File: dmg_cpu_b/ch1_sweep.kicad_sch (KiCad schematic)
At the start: 109 parts

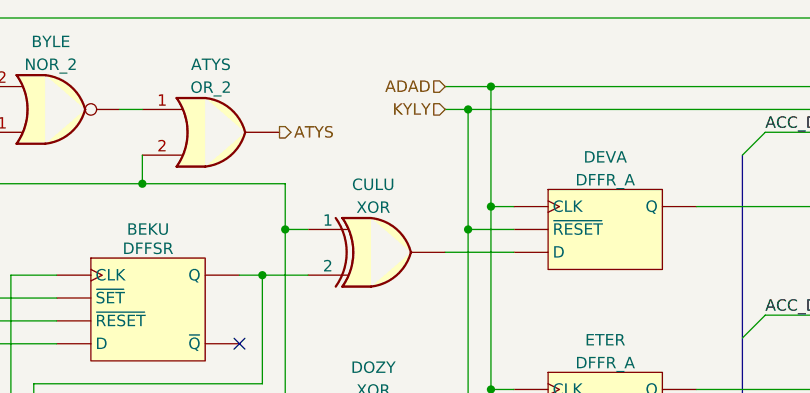
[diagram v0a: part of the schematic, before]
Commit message: Channel 2 + Channel 3 added. Channel 3 fits on 2 sheets.
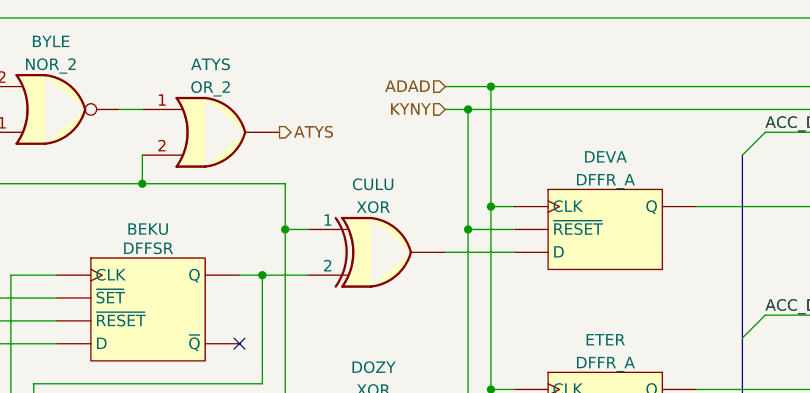
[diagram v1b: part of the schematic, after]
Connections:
- net KYLY renamed KYNY
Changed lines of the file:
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@@
     (effects (font (size 1.27 1.27)) (justify left))
   )
-  (hierarchical_label "KYLY" (shape input) (at 246.38 23.495 180)
+  (hierarchical_label "KYNY" (shape input) (at 246.38 23.495 180)
     (effects (font (size 1.27 1.27)) (justify right))
   )

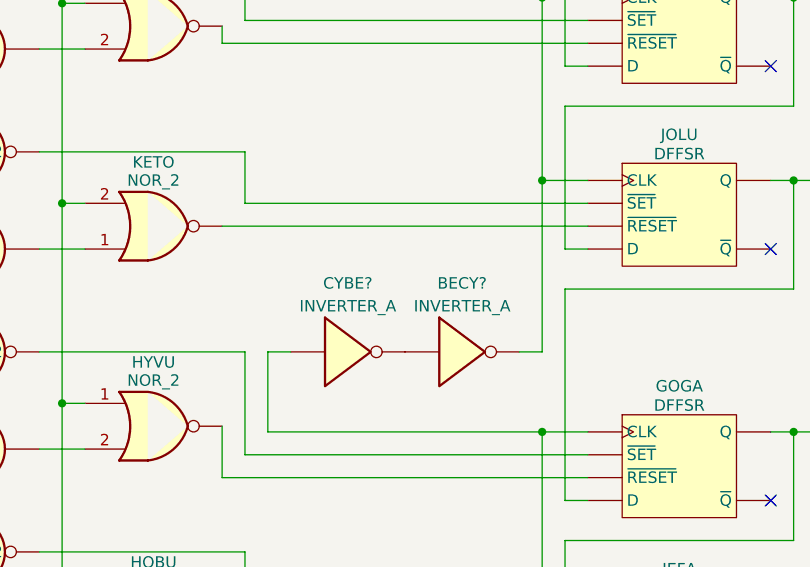
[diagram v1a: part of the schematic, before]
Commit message: fixes made following review
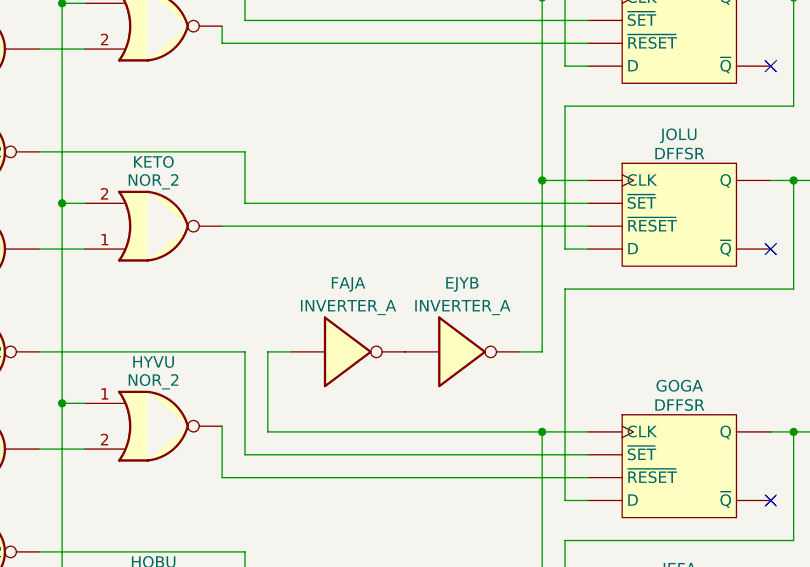
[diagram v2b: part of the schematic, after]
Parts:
- gave numbers to parts that had none: 2
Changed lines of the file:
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@@
   (symbol (lib_id "DMG_CPU_Cells:INVERTER_A") (at 176.53 210.82 0) (unit 1)
     (in_bom yes) (on_board yes)
-    (property "Reference" "CYBE?" (id 0) (at 176.53 203.2 0))
+    (property "Reference" "FAJA" (id 0) (at 176.53 203.2 0))
     (property "Value" "INVERTER_A" (id 1) (at 176.53 205.74 0))
     (property "Footprint" "" (id 2) (at 173.99 210.82 0)
@@
   (symbol (lib_id "DMG_CPU_Cells:INVERTER_A") (at 189.23 210.82 0) (unit 1)
     (in_bom yes) (on_board yes)
-    (property "Reference" "BECY?" (id 0) (at 189.23 203.2 0))
+    (property "Reference" "EJYB" (id 0) (at 189.23 203.2 0))
     (property "Value" "INVERTER_A" (id 1) (at 189.23 205.74 0))
     (property "Footprint" "" (id 2) (at 186.69 210.82 0)

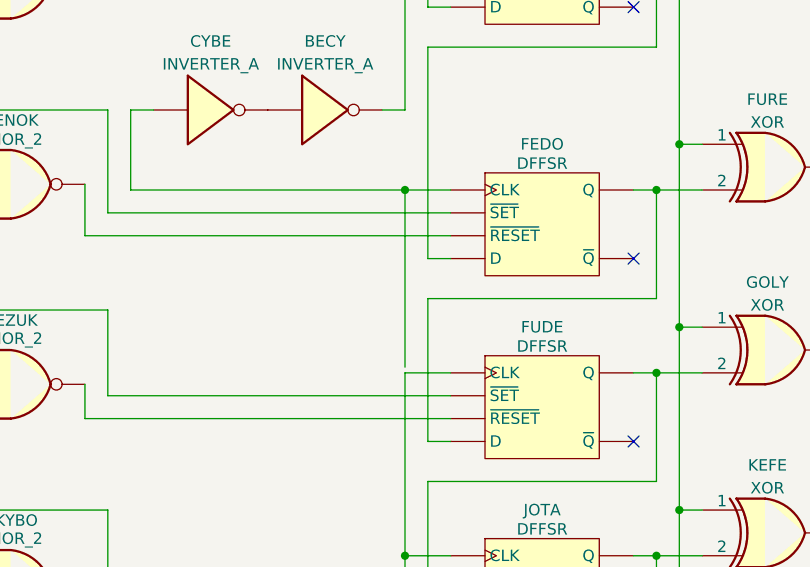
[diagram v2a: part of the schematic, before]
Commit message: Fixes made from issues, channel 4 sheet aded and tidy up of hierarchical APU sheet. Small fixes done here and there when doing ERC.
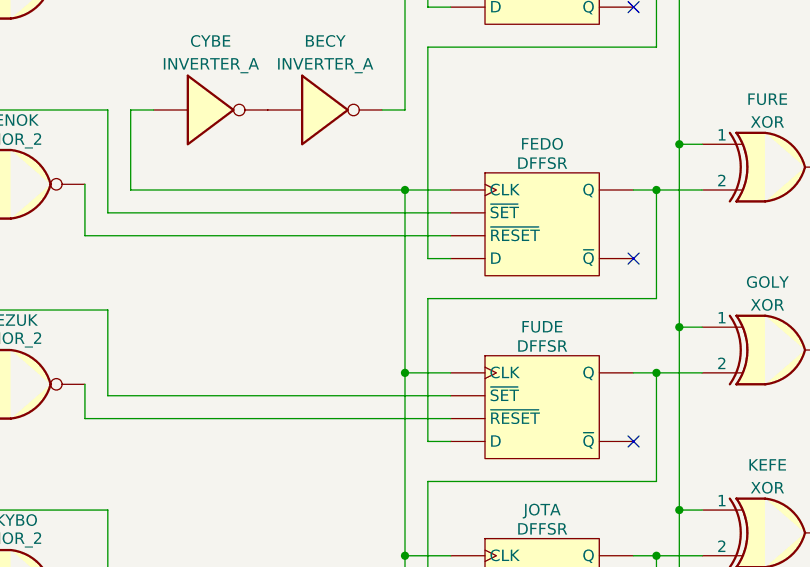
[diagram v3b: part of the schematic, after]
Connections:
- net at CYBE.1, FEDO.7 (CLK): now also EJYB.2, FUDE.7 (CLK), JOLU.7 (CLK), JOTA.7 (CLK)
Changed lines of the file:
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@@
   (junction (at 294.005 81.915) (diameter 0) (color 0 0 0 0)
+  )
+  (junction (at 198.12 151.13) (diameter 0) (color 0 0 0 0)
   )
   (junction (at 294.005 61.595) (diameter 0) (color 0 0 0 0)
@@
     (stroke (width 0) (type default) (color 0 0 0 0))
   )
-  (wire (pts (xy 198.12 130.81) (xy 198.12 150.495))
+  (wire (pts (xy 198.12 130.81) (xy 198.12 151.13))
     (stroke (width 0) (type default) (color 0 0 0 0))
   )
@@
   (symbol (lib_id "power:GND") (at 192.405 52.07 0) (unit 1)
     (in_bom yes) (on_board yes) (fields_autoplaced)
-    (property "Reference" "#PWR?" (id 0) (at 192.405 58.42 0)
+    (property "Reference" "#PWR0108" (id 0) (at 192.405 58.42 0)
       (effects (font (size 1.27 1.27)) hide)
     )

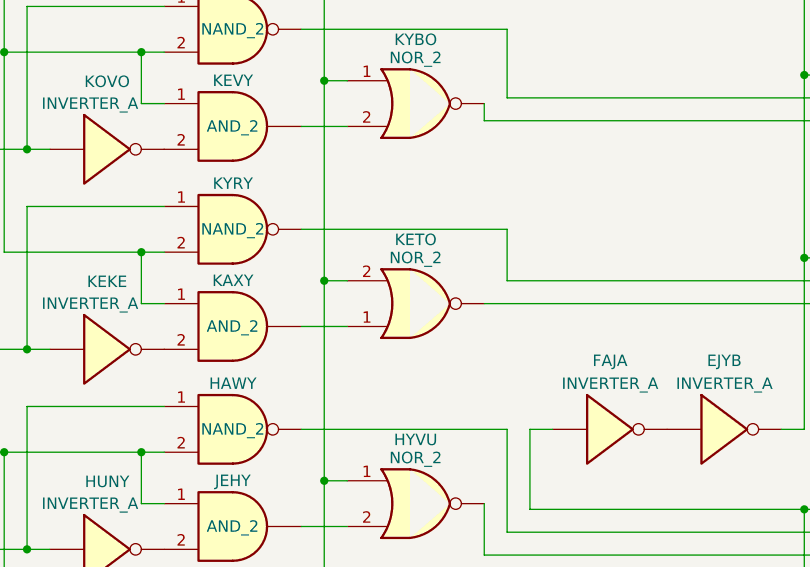
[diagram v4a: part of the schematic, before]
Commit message: Fixes made based on raised issues. PPU decode page added as draft level.
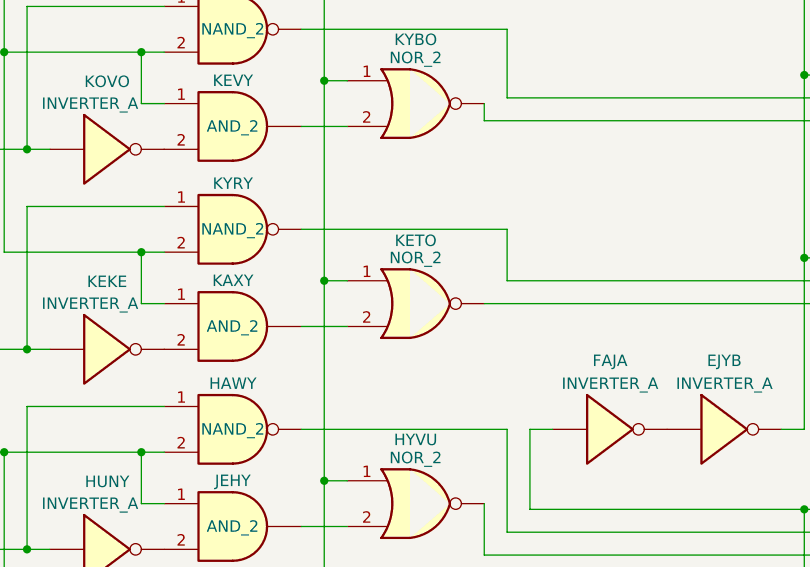
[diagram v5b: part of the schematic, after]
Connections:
- net APU_RESET: now also KETO.1; no longer KETO.2
- net at KAXY.3: now also KETO.2; no longer KETO.1
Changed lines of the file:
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@@
     (pin "2")
   )
-  (symbol (lib_id "DMG_CPU_Cells:NOR_2") (at 154.94 196.85 0) (mirror x) (unit 1)
+  (symbol (lib_id "DMG_CPU_Cells:NOR_2") (at 154.94 196.85 0) (unit 1)
     (in_bom yes) (on_board yes)
-    (property "Reference" "KETO" (id 0) (at 154.9398 189.7579 0))
+    (property "Reference" "KETO" (id 0) (at 154.94 189.865 0))
     (property "Value" "NOR_2" (id 1) (at 154.94 191.77 0))
     (property "Footprint" "" (id 2) (at 154.686 196.85 0)
       (effects (font (size 1.27 1.27)) hide)
     )
-    (property "Datasheet" "http://iceboy.a-singer.de/doc/dmg_cells.html#nor2" (id 3) (at 154.94 189.23 0)
+    (property "Datasheet" "http://iceboy.a-singer.de/doc/dmg_cells.html#nor2" (id 3) (at 154.94 204.47 0)
       (effects (font (size 1.27 1.27)) hide)
     )

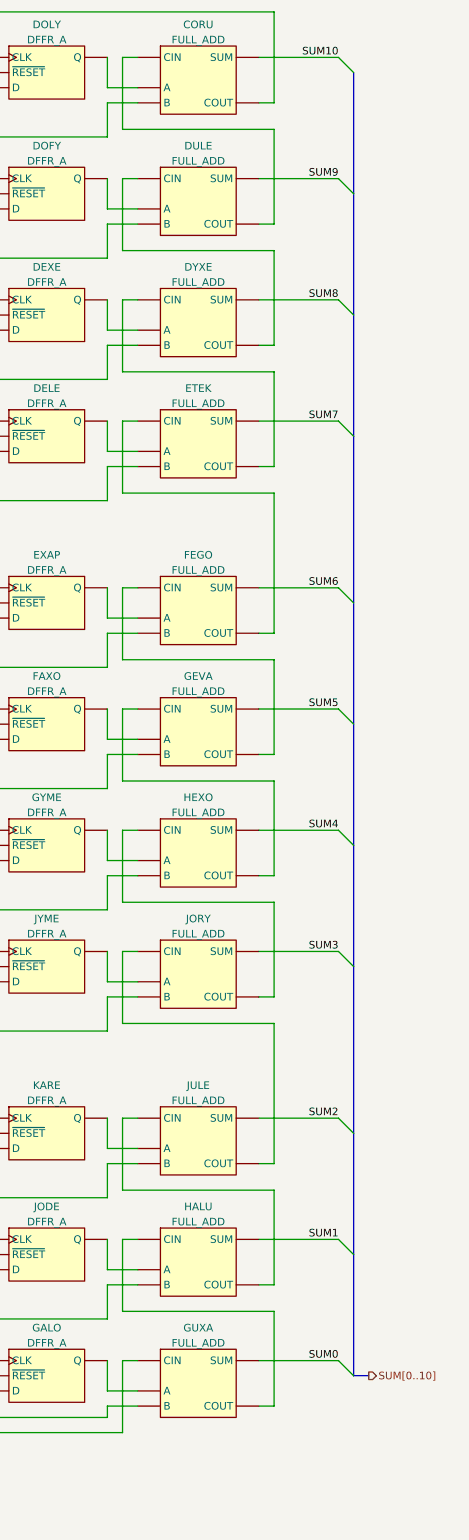
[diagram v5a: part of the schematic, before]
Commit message: Fixes and and rearranged schematics whereever possible to improve legibility.
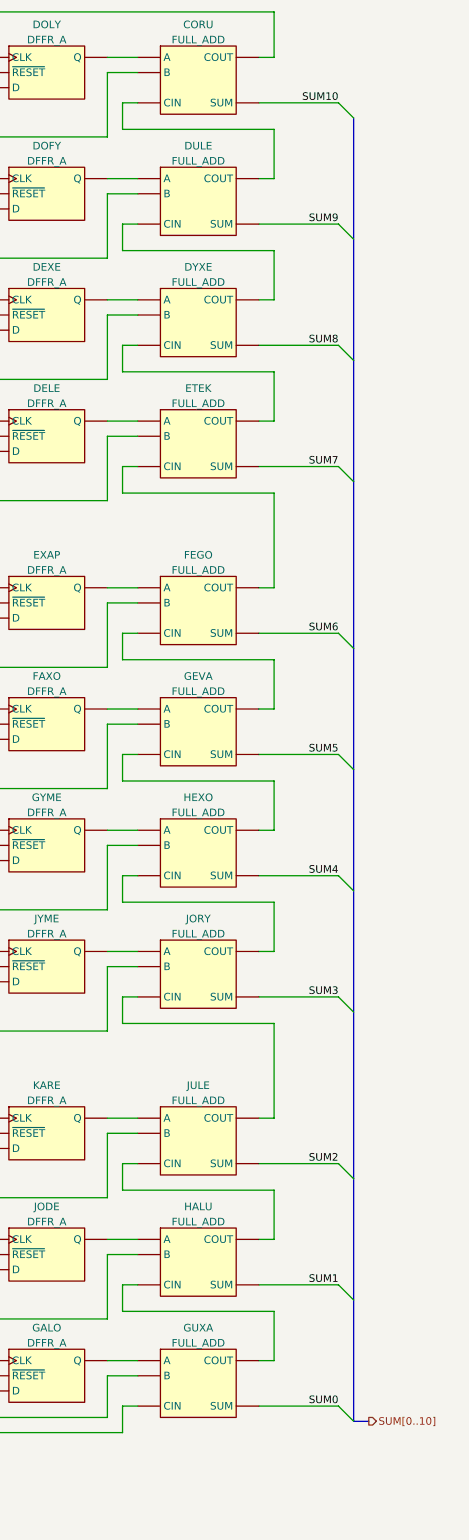
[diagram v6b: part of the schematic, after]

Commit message: VRAM interface sheet added but various edits in existing sheets. Notable merge of RESET, CLOCKS and FF04 DIV sheets
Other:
- company: (none) -> CC-BY-SA-4.0 Régis Galland & Michael Singer -- Derived work from Furrtek
- title: (none) -> DMG CPU B
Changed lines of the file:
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@@
 (kicad_sch (version 20211123) (generator eeschema)
   (paper "A3")
+  (title_block
+    (title "DMG CPU B")
+    (date "2022-05-02")
+    (rev "0")
+    (company "CC-BY-SA-4.0 Régis Galland & Michael Singer -- Derived work from Furrtek")
+    (comment 1 "https://github.com/msinger/dmg-schematics")
+  )
   (junction (at 228.6 57.15) (diameter 0) (color 0 0 0 0)
   )

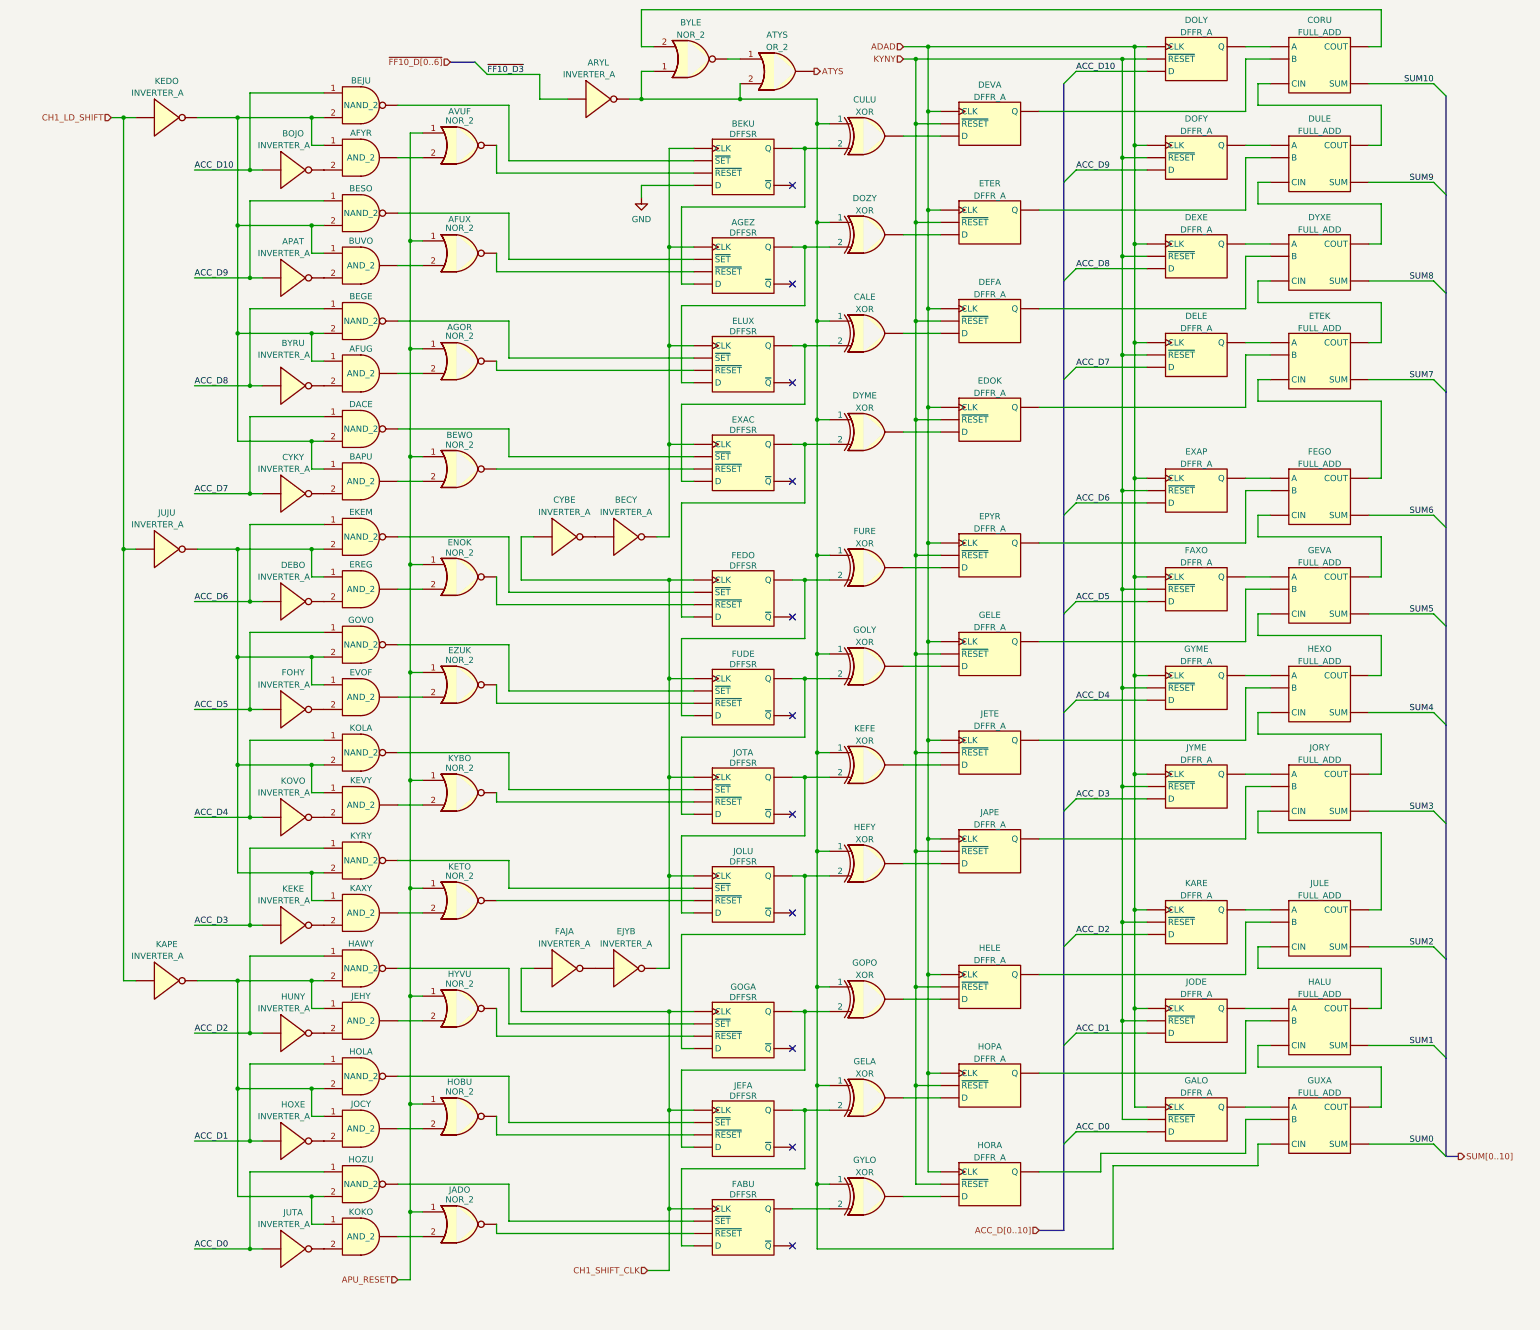
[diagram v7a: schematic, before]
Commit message: All sheets captured. Serious tidying is required in PPU section.
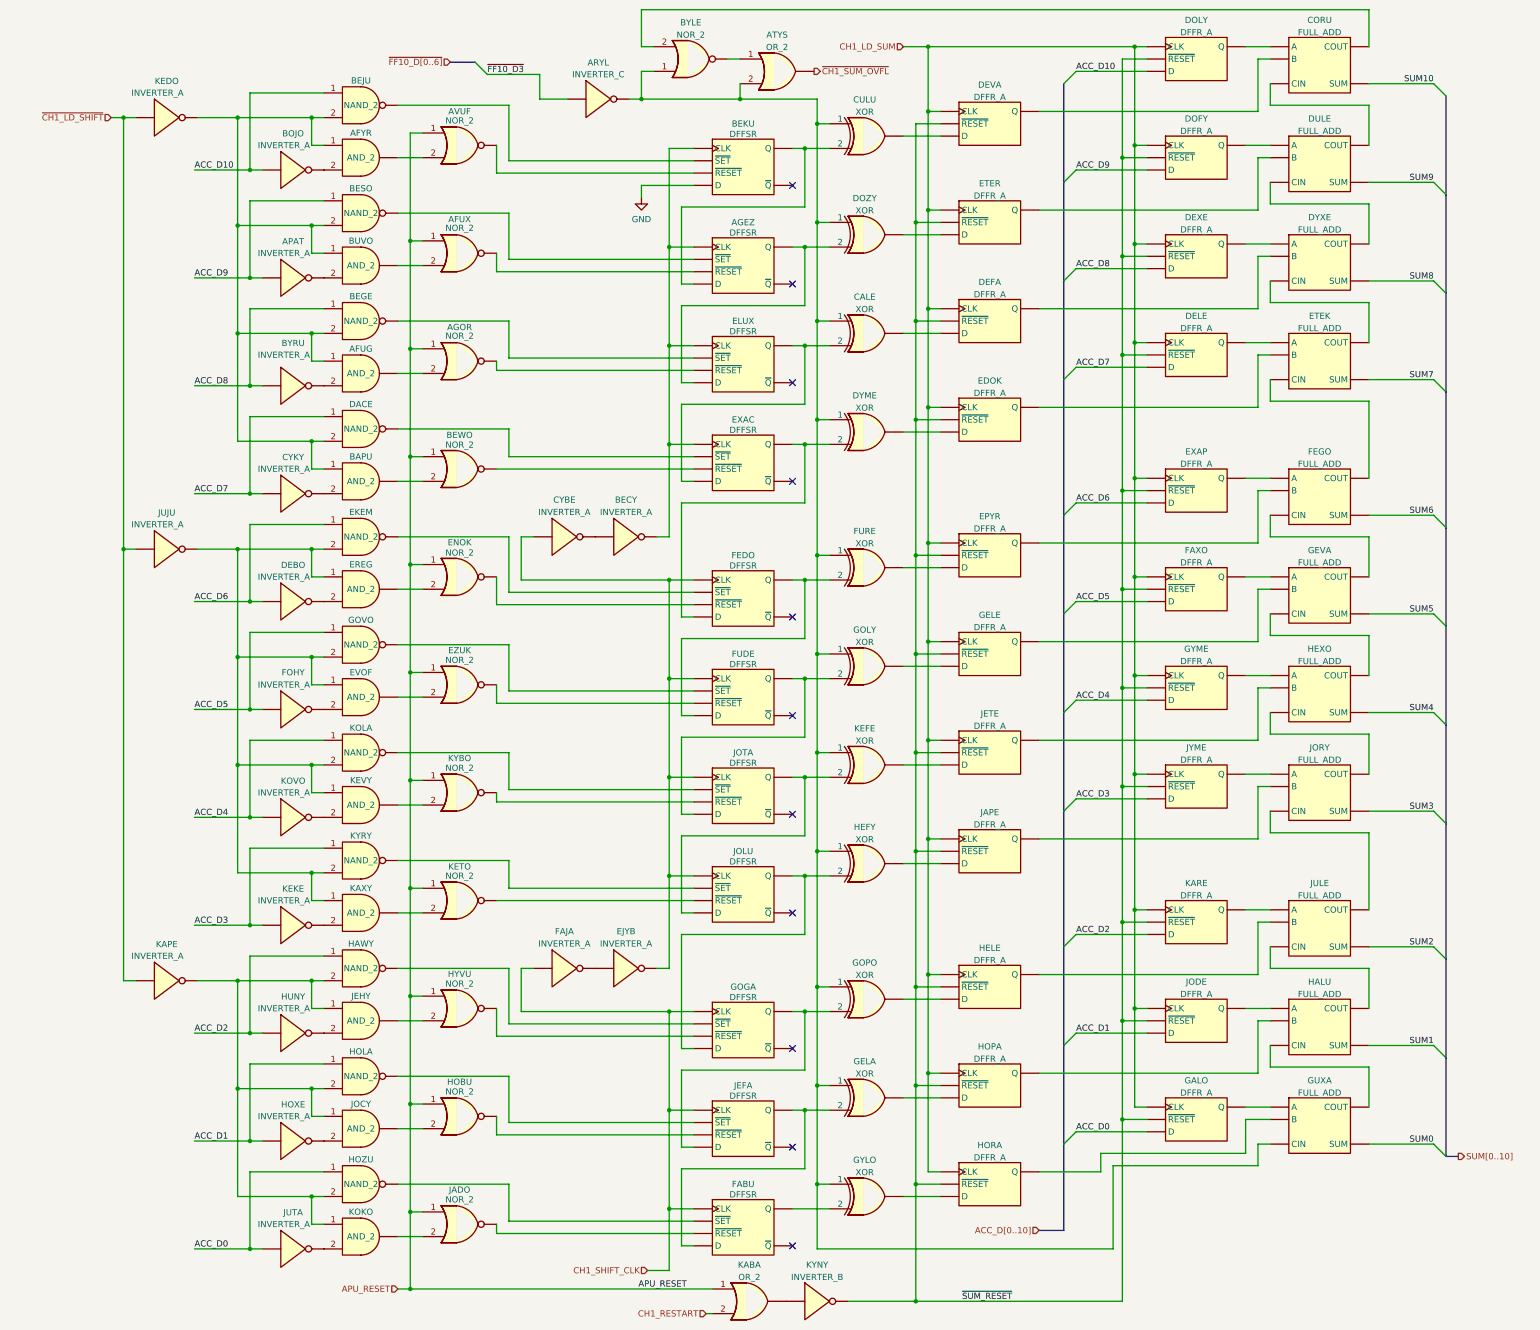
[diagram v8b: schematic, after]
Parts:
- added KABA: OR_2, symbol DMG_CPU_Cells:OR_2
- added KYNY: INVERTER_B, symbol DMG_CPU_Cells:INVERTER_B
- ARYL: value INVERTER_A -> INVERTER_C; symbol DMG_CPU_Cells:INVERTER_A -> DMG_CPU_Cells:INVERTER_C
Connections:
- net APU_RESET: now also KABA.1
- net ADAD renamed CH1_LD_SUM
- net ATYS renamed ~{CH1_SUM_OVFL}
- net CH1_LD_SHIFT renamed ~{CH1_LD_SHIFT}
- net KYNY renamed ~{SUM_RESET}
- net ~{SUM_RESET}: now also KYNY.2
- new net: KABA.3, KYNY.1
- new net CH1_RESTART: KABA.2
